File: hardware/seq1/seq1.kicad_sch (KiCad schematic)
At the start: 43 parts, among them J1 AudioJack2_SwitchT, J2 AudioJack2_SwitchT, J4 Conn_02x08_Odd_Even, SW1 SW_Push, SW10 SW_Push, SW11 SW_Push, SW2 SW_Push, SW3 SW_Push, SW4 SW_Push, SW5 SW_Push, SW6 SW_Push, SW7 SW_Push, SW8 SW_Push, SW9 PEC12R-3220F-S0024, U1 TLV2372, U2 74HC4051, U3 74HC4051, U4 Adafruit QTPy SAMD21, U5 128x64 0.96" OLED I2C

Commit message: firmware draft for sequencer, tested buttons and pots through the muxes, verified ADC config
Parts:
- removed U1: TLV2372, symbol Amplifier_Operational:TLV2372
- added D9: SS16, Diode_SMD:D_SMA, symbol Diode:SS16
- added U1: 74HCT1G125GW, Package_TO_SOT_SMD:SOT-353_SC-70-5_Handsoldering, symbol 74xGxx:74AHCT1G125
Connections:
- net +3V3: no longer D1.1 (VDD), D2.1 (VDD), D3.1 (VDD), D4.1 (VDD), D5.1 (VDD), D6.1 (VDD), D7.1 (VDD), D8.1 (VDD), SW1.2, SW2.2, SW3.2, SW4.2, SW5.2, SW6.2, SW7.2, SW8.2
- net +5V: now also D1.1 (VDD), D2.1 (VDD), D3.1 (VDD), D4.1 (VDD), D5.1 (VDD), D6.1 (VDD), D7.1 (VDD), D8.1 (VDD), D9.1 (K), U1.5 (VCC); no longer J4.11 (Pin_11), J4.12 (Pin_12)
- net GATE: now also U4.8 (D7/A7/RX/PA07); no longer U4.2 (D1/A1/PA03)
- net GND: now also SW1.2, SW2.2, SW3.2, SW4.2, SW5.2, SW6.2, SW7.2, SW8.2, SW9.C, SW9.S2, U1.1, U1.3 (GND); no longer SW9.S1
- net at SW7.1: now also U2.5 (A5); no longer U2.2 (A6)
- net at RV7.2: now also U3.5 (A5); no longer U3.2 (A6)
- net at SW6.1: now also U2.4 (A7); no longer U2.5 (A5)
- net at RV4.2: now also U3.15 (A2); no longer U3.12 (A3)
- net at SW5.1: now also U2.2 (A6); no longer U2.1 (A4)
- net at RV3.2: now also U3.12 (A3); no longer U3.15 (A2)
- net at RV8.2: now also U3.1 (A4); no longer U3.4 (A7)
- net at U2.12 (A3): now also SW3.1; no longer SW4.1
- net at U2.15 (A2): now also SW4.1; no longer SW3.1
- net at SW8.1: now also U2.1 (A4); no longer U2.4 (A7)
- net at U4.10 (D9/A9/MISO/PA09): now also R3.1; no longer R4.1
- net NPXL_D: now reaches U4.11 (D10/A10/MOSI/PA10)
- net NPXL_D: now also U1.2; no longer R3.1
- net at U4.9 (D8/A8/SCK/PA11): now also R4.1; no longer SW9.S2
- net at RV5.2: now also U3.2 (A6); no longer U3.1 (A4)
- net at RV6.2: now also U3.4 (A7); no longer U3.5 (A5)
- net NEOPXL_DATA: no longer names the net of D1.4 (DIN)
- net NEOPXL_DATA: now also U1.4; no longer U4.8 (D5/A7/RX/PA07)
- net SW_DATA renamed SW_MUX
- net VR_VAL renamed POT_MUX
- net POT_MUX: now also U4.2 (D1/A1/PA03); no longer U4.7 (D6/A6/TX/PA06)
- new net: D9.2 (A), J4.11 (Pin_11), J4.12 (Pin_12)
- new net ROT_SW: SW9.S1, U4.7 (D6/A6/TX/PA06)
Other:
- added sheet seq1-alt-mcu (seq1-alt-mcu.kicad_sch)
- note added: "Gray code ordering 0: 000 - 0 1: 001 - 1 2: 011 - 3 3: 010 - 2 4: 110 - 6 5: 111 - 7 6: 101 - 5 7: 100 - 4"
- moved on the sheet: C1, C2, R1, R2, R3, R4, SW9

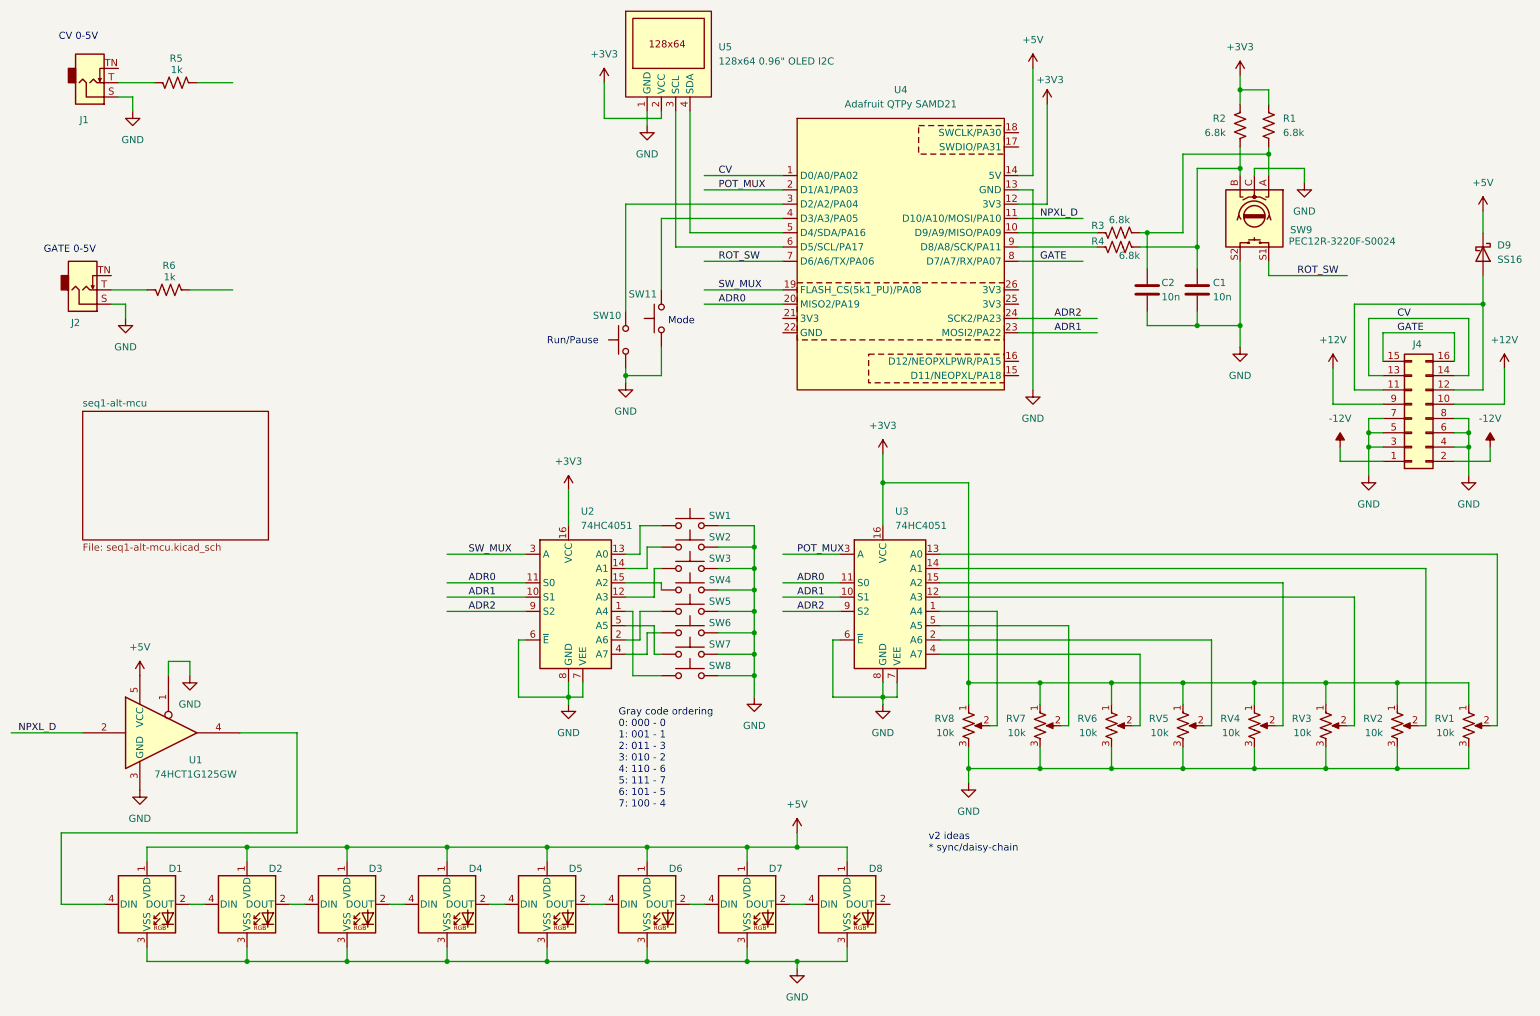
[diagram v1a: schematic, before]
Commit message: updates to schematic/layout (started layout). Added glyph and display class to manage and show status (PoC)
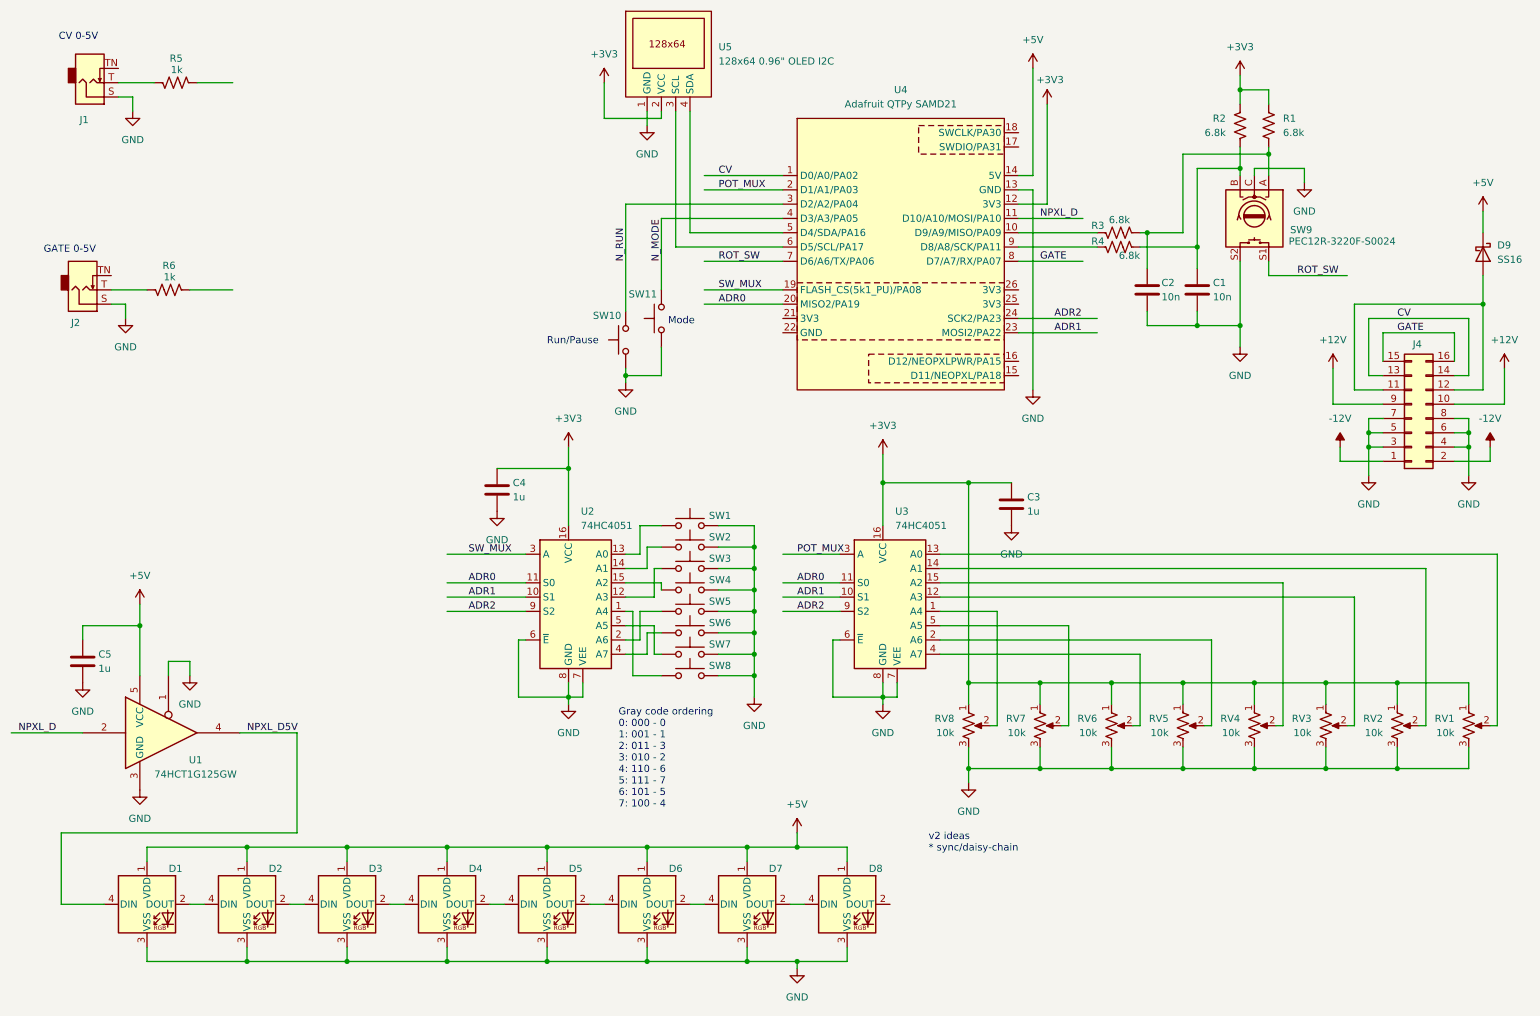
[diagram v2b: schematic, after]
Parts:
- added C3, C4, C5: 1u, Capacitor_THT:C_Disc_D5.0mm_W2.5mm_P5.00mm, symbol Device:C
- C1, C2: footprint (none) -> Capacitor_THT:C_Disc_D5.0mm_W2.5mm_P5.00mm
- D2, D3, D4, D5, D6, D7, D8: footprint LED_SMD:LED_WS2812B_PLCC4_5.0x5.0mm_P3.2mm -> LED_SMD:LED_WS2812B-2020_PLCC4_2.0x2.0mm
- R1, R2, R3, R4: footprint (none) -> Resistor_THT:R_Axial_DIN0207_L6.3mm_D2.5mm_P10.16mm_Horizontal
- U2, U3: footprint (none) -> Package_DIP:DIP-16_W7.62mm_Socket
- U4: footprint (none) -> Module_Custom:Adafruit_QtPY_SAMD21
- U5: footprint (none) -> Display_Custom:OLED_0.96in_SSD1306_I2C
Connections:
- net +3V3: now also C3.1, C4.1
- net +5V: now also C5.1
- net GND: now also C3.2, C4.2, C5.2
- net NPXL_D5V: now reaches D1.4 (DIN), U1.4
- net N_RUN: now reaches SW10.2, U4.3 (D2/A2/PA04)
- net N_MODE: now reaches SW11.2, U4.4 (D3/A3/PA05)
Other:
- removed sheet seq1-alt-mcu

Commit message: menu system and adjustment through the physical interface
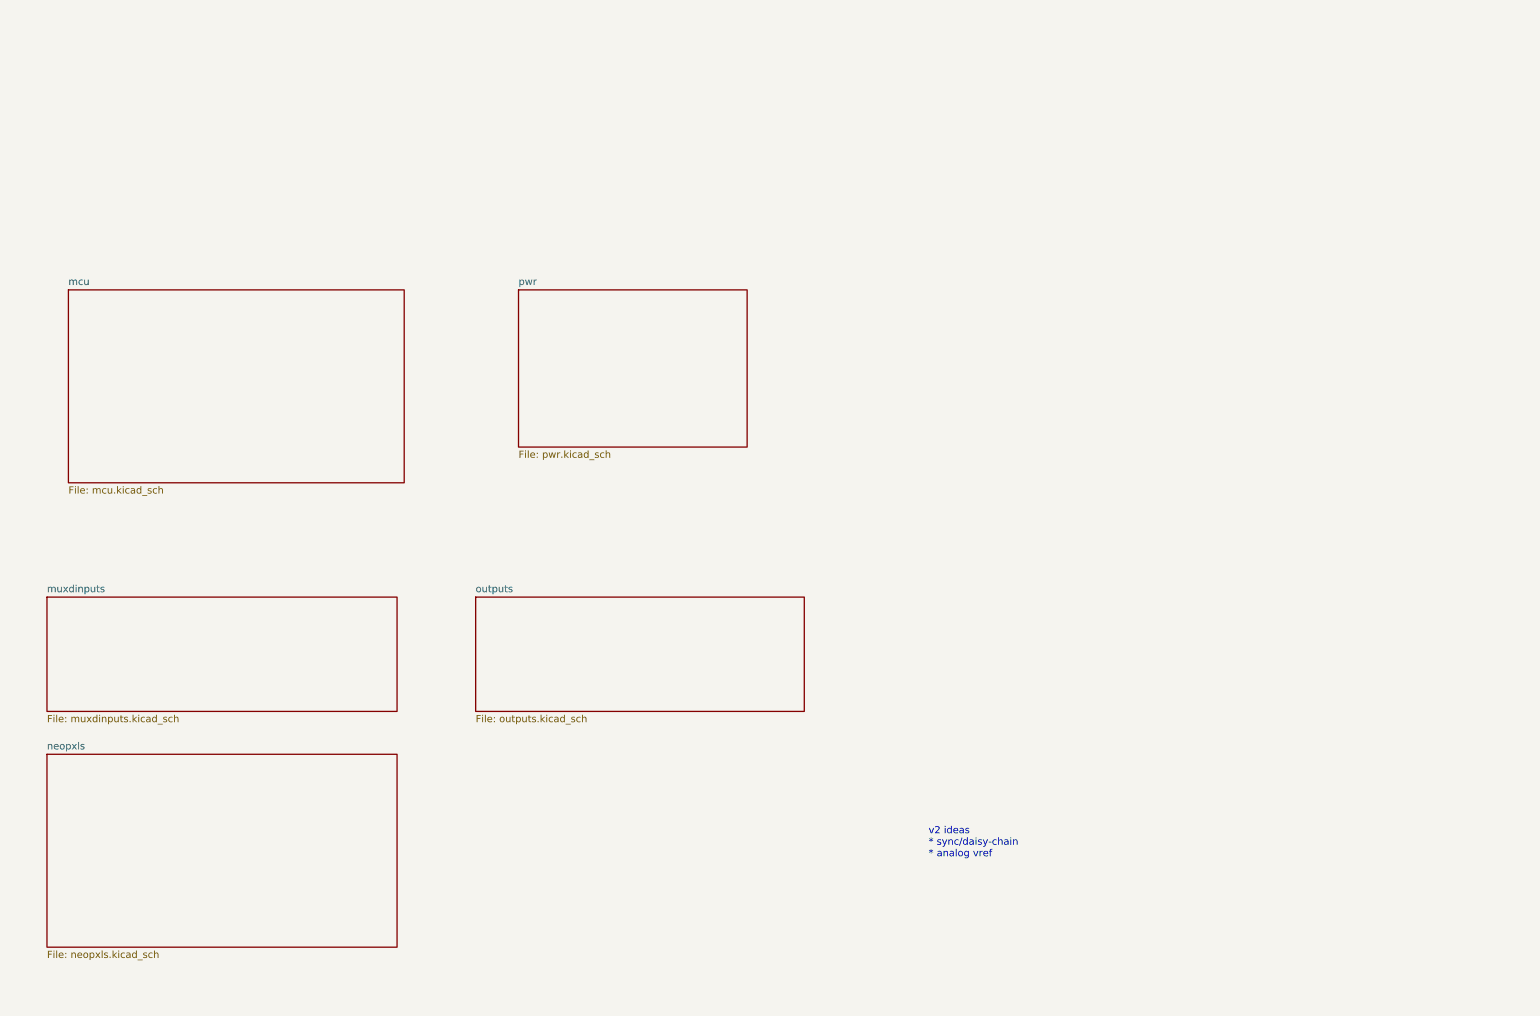
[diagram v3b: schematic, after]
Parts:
- removed C1, C2: 10n, Capacitor_THT:C_Disc_D5.0mm_W2.5mm_P5.00mm, symbol Device:C
- removed C3, C4, C5: 1u, Capacitor_THT:C_Disc_D5.0mm_W2.5mm_P5.00mm, symbol Device:C
- removed D1, D2, D3, D4, D5, D6, D7, D8: WS2812B, LED_SMD:LED_WS2812B-2020_PLCC4_2.0x2.0mm, symbol LED:WS2812B
- removed D9: SS16, Diode_SMD:D_SMA, symbol Diode:SS16
- removed J1, J2: AudioJack2_SwitchT, symbol Connector_Audio:AudioJack2_SwitchT
- removed J4: Conn_02x08_Odd_Even, Connector_IDC:IDC-Header_2x08_P2.54mm_Vertical, symbol Connector_Generic:Conn_02x08_Odd_Even
- removed R1, R2, R3, R4: 6.8k, Resistor_THT:R_Axial_DIN0207_L6.3mm_D2.5mm_P10.16mm_Horizontal, symbol Device:R_US
- removed R5, R6: 1k, symbol Device:R_US
- removed RV1, RV2, RV3, RV4, RV5, RV6, RV7, RV8: 10k, Potentiometer_THT:Potentiometer_Bourns_PTV09A-1_Single_Vertical, symbol Device:R_Potentiometer_US
- removed SW1, SW10, SW11, SW2, SW3, SW4, SW5, SW6, SW7, SW8: SW_Push, Button_Switch_THT:SW_PUSH_6mm_H5mm, symbol Switch:SW_Push
- removed SW9: PEC12R-3220F-S0024, Rotary_Encoder:RotaryEncoder_Bourns_Vertical_PEC12R-3x17F-Sxxxx, symbol Device:RotaryEncoder_Switch
- removed U1: 74HCT1G125GW, Package_TO_SOT_SMD:SOT-353_SC-70-5_Handsoldering, symbol 74xGxx:74AHCT1G125
- removed U2, U3: 74HC4051, Package_DIP:DIP-16_W7.62mm_Socket, symbol 74xx:74HC4051
- removed U4: Adafruit QTPy SAMD21, Module_Custom:Adafruit_QtPY_SAMD21, symbol MCU_Module_Custom:Adafruit_QTPy_SAMD21
- removed U5: 128x64 0.96" OLED I2C, Display_Custom:OLED_0.96in_SSD1306_I2C, symbol MCU_Module_Custom:128x64_OLED_I2C_Module
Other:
- added sheet mcu (mcu.kicad_sch)
- added sheet muxdinputs (muxdinputs.kicad_sch)
- added sheet neopxls (neopxls.kicad_sch)
- added sheet outputs (outputs.kicad_sch)
- added sheet pwr (pwr.kicad_sch)
- note added: "v2 ideas * sync/daisy-chain * analog vref"
- note removed: "CV 0-5V"
- note removed: "GATE 0-5V"
- note removed: "Gray code ordering 0: 000 - 0 1: 001 - 1 2: 011 - 3 3: 010 - 2 4: 110 - 6 5: 111 - 7 6: 101 - 5 7: 100 - 4"
- note removed: "Mode"
- note removed: "Run/Pause"
- note removed: "v2 ideas * sync/daisy-chain"

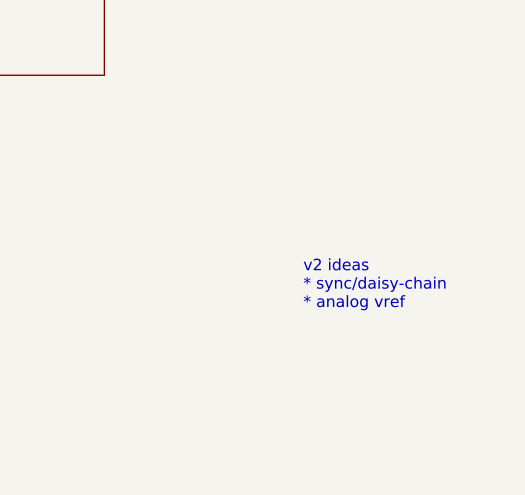
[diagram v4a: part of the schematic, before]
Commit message: updating the board with new line in
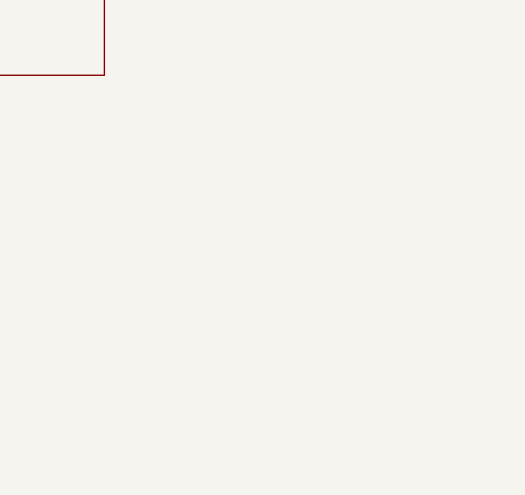
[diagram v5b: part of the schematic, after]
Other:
- note removed: "v2 ideas * sync/daisy-chain * analog vref"
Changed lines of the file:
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@@
 	(generator "eeschema")
 	(generator_version "8.0")
-	(paper "A4")
+	(paper "USLetter")
 	(title_block
 		(title "Sequencer")
-		(date "2024-03-18")
-		(rev "0.1")
+		(date "2024-10-14")
+		(rev "1.1")
 		(company "idyllm")
-	)
-	(text "v2 ideas\n* sync/daisy-chain\n* analog vref"
-		(exclude_from_sim no)
-		(at 178.308 169.418 0)
-		(effects
-			(font
-				(size 1.27 1.27)
-			)
-			(justify left)
-		)
+		(comment 1 "CC BY-SA 4.0")
+		(comment 2 "References: Korg SQ-1")
 	)
 	(sheet
